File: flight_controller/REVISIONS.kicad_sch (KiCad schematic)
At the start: 21 parts, among them U10 ESD7104MUTAG_C2987068, U11 STM32H753IIT6, U7 ESD7104MUTAG_C2987068, U8 ESD7104MUTAG_C2987068, U9 ESD7104MUTAG_C2987068

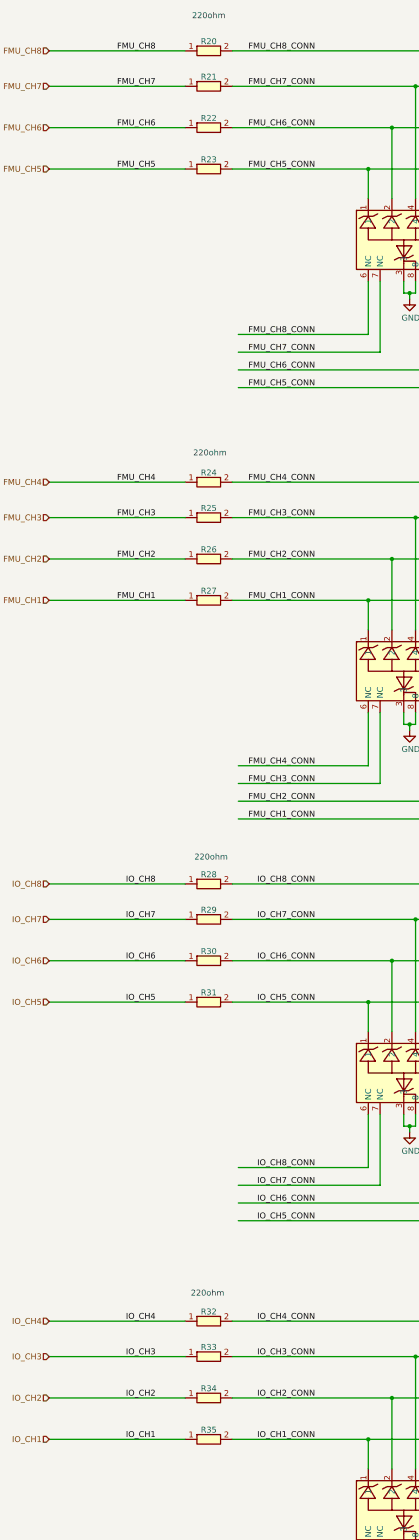
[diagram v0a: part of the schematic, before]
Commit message: updating symbols as in the shared library
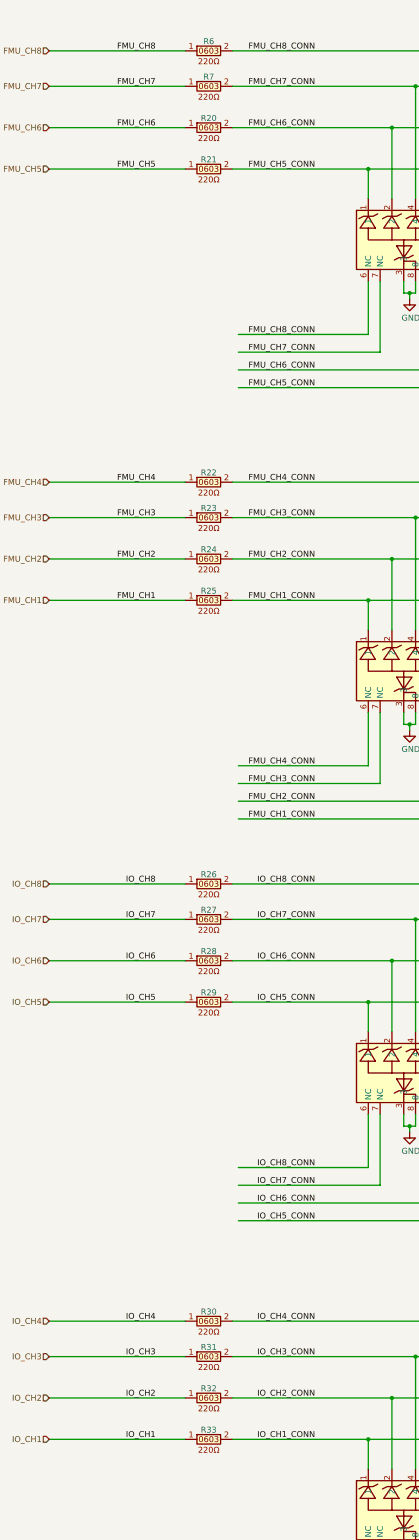
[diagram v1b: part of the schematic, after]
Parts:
- removed R20, R21, R22, R23, R24, R25, R26, R27, R28, R29, R30, R31, R32, R33, R34, R35: 0603WAF2200T5E, easyeda2kicad:R0603, symbol lampelKicadLIB:0603WAF2200T5E
- added R20, R21, R22, R23, R24, R25, R26, R27, R28, R29, R30, R31, R32, R33, R6, R7: 0603WAF2200T5E (220ohm , 0603), easyeda2kicad:R0603, symbol lampelKicadLIB:0603WAF2200T5E (220ohm , 0603)
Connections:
- net FMU_CH1: now also R25.1
- net FMU_CH1_CONN: now also R25.2
- net FMU_CH2: now also R24.1
- net FMU_CH2_CONN: now also R24.2
- net FMU_CH3: now also R23.1
- net FMU_CH3_CONN: now also R23.2
- net FMU_CH4: now also R22.1
- net FMU_CH4_CONN: now also R22.2
- net FMU_CH5: now also R21.1
- net FMU_CH5_CONN: now also R21.2
- net FMU_CH6: now also R20.1
- net FMU_CH6_CONN: now also R20.2
- net FMU_CH7: now also R7.1
- net FMU_CH7_CONN: now also R7.2
- net FMU_CH8: now also R6.1
- net FMU_CH8_CONN: now also R6.2
- net IO_CH1: now also R33.1
- net IO_CH1_CONN: now also R33.2
- net IO_CH2: now also R32.1
- net IO_CH2_CONN: now also R32.2
- net IO_CH3: now also R31.1
- net IO_CH3_CONN: now also R31.2
- net IO_CH4: now also R30.1
- net IO_CH4_CONN: now also R30.2
- net IO_CH5: now also R29.1
- net IO_CH5_CONN: now also R29.2
- net IO_CH6: now also R28.1
- net IO_CH6_CONN: now also R28.2
- net IO_CH7: now also R27.1
- net IO_CH7_CONN: now also R27.2
- net IO_CH8: now also R26.1
- net IO_CH8_CONN: now also R26.2
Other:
- note removed: "220ohm"

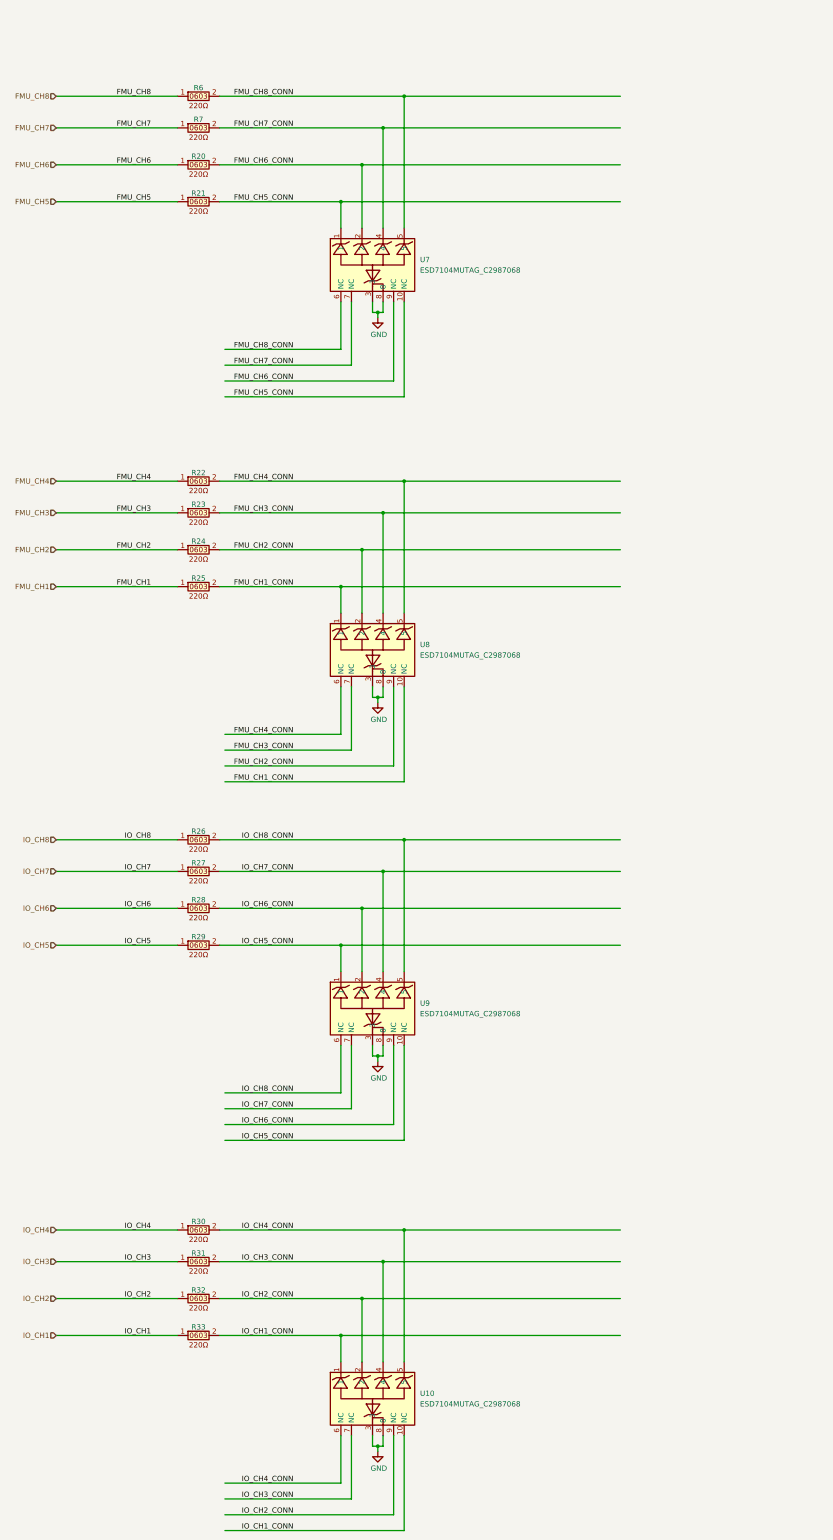
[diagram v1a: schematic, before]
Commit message: gps and power blocks
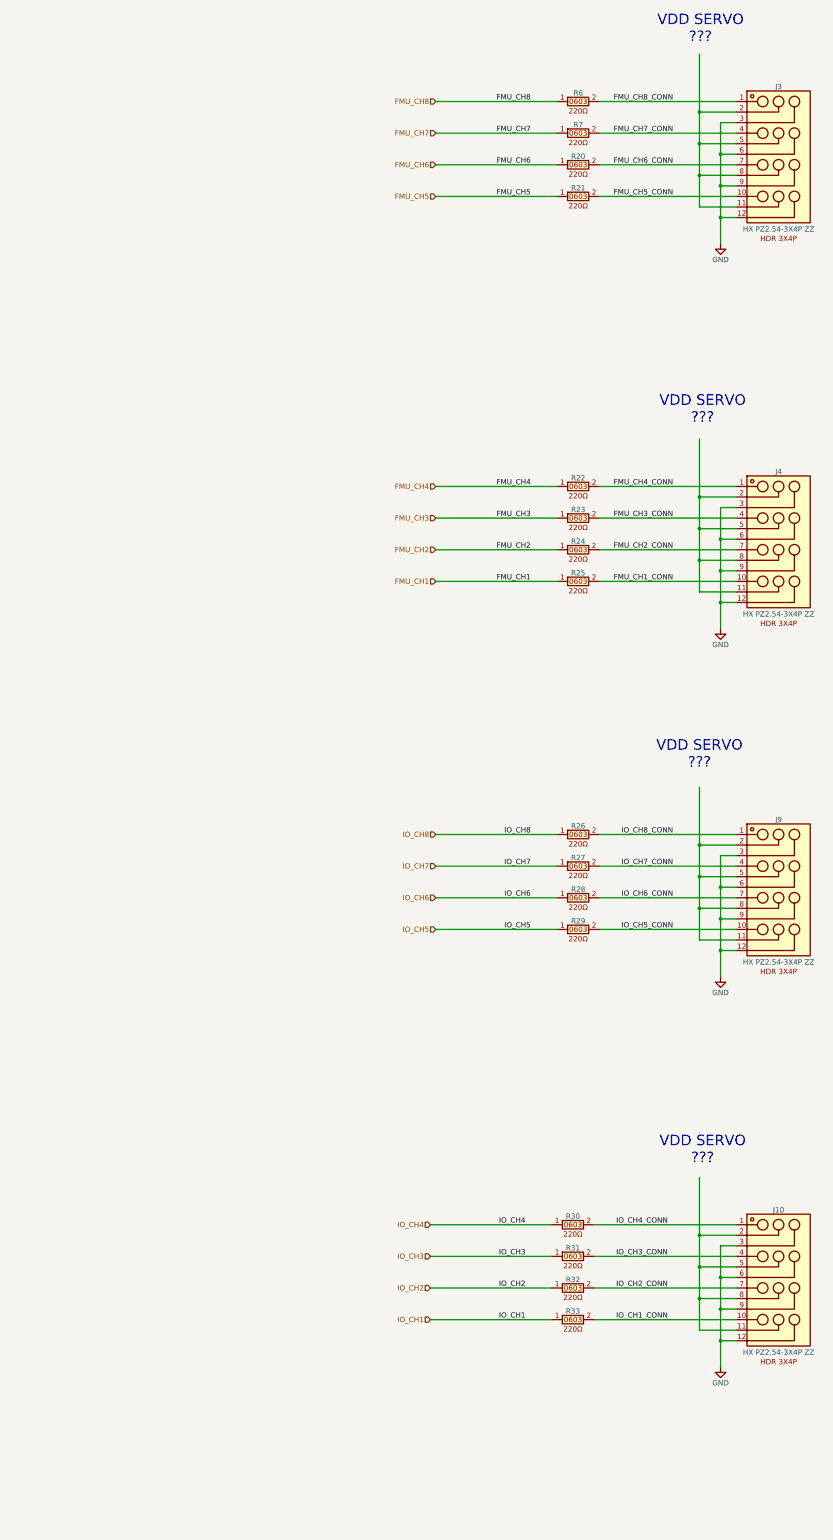
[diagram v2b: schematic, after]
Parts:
- removed U10, U7, U8, U9: ESD7104MUTAG_C2987068, easyeda2kicad:DFN-10_L2.5-W1.0-P0.50-BL, symbol easyeda2kicad:ESD7104MUTAG_C2987068
- added J10, J3, J4, J9: HX PZ2.54-3X4P ZZ, easyeda2kicad:HDR-TH_12P-P2.54-V-M-R3-C4-S2.54, symbol lampelKicadLIB:HXPZ2.54-3X4PZZ
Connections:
- net FMU_CH1_CONN: now also J4.10
- net FMU_CH2_CONN: now also J4.7
- net FMU_CH3_CONN: now also J4.4
- net FMU_CH4_CONN: now also J4.1
- net FMU_CH5_CONN: now also J3.10
- net FMU_CH6_CONN: now also J3.7
- net FMU_CH7_CONN: now also J3.4
- net FMU_CH8_CONN: now also J3.1
- net GND: now also J10.12, J10.3, J10.6, J10.9, J3.12, J3.3, J3.6, J3.9, J4.12, J4.3, J4.6, J4.9, J9.12, J9.3, J9.6, J9.9
- net IO_CH1_CONN: now also J10.10
- net IO_CH2_CONN: now also J10.7
- net IO_CH3_CONN: now also J10.4
- net IO_CH4_CONN: now also J10.1
- net IO_CH5_CONN: now also J9.10
- net IO_CH6_CONN: now also J9.7
- net IO_CH7_CONN: now also J9.4
- net IO_CH8_CONN: now also J9.1
- new net: J3.11, J3.2, J3.5, J3.8
- new net: J4.11, J4.2, J4.5, J4.8
- new net: J9.11, J9.2, J9.5, J9.8
- new net: J10.11, J10.2, J10.5, J10.8
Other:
- note added: "VDD SERVO ???"
- moved on the sheet: R20, R21, R22, R23, R24, R25, R26, R27, R28, R29, R30, R31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
